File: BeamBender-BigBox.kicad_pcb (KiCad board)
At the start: 4 copper layers, 157.5 x 90 mm, 126 parts, among them CN1 A4000-CN621-36, CN2 A4000-CN622-54, J1 HDMI, J2 JTAG, J3 JTAG_Pogo, J4 EXT_BUTTONS, SW1 MENU, SW2 UP, SW3 DOWN, U1 Colorlight-i5-v7.0, U2 TLV76133DCYR, U3 74LVC16244ADGG, U4 74LVC16244ADGG, U5 SII9022ACNU, U6 74LVC1G86, U7 AK5720VT, U8 AP2112K-1.2, X1 Oscillator_3.2x2.5mm-27MHz, X2 Oscillator_5.0x3.2mm_24.576MHz

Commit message: Add R0/R1 pull down resistors
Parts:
- removed REF**: OSHW-Logo2_9.8x8mm_SilkScreen, Symbol:OSHW-Logo2_9.8x8mm_SilkScreen
- removed REF**: OSHW-Logo_11.4x12mm_SilkScreen, Symbol:OSHW-Logo_11.4x12mm_SilkScreen
- added R43: 100K, Resistor_SMD:R_0603_1608Metric, F.Cu at (133.2, 67.5)
- added R44: 100K, Resistor_SMD:R_0603_1608Metric, F.Cu at (133.2, 65.9)
- C18, C19: value 10uF X7R 1206 -> 10uF 1206
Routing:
- net R1: track 40.1 -> 45.3 mm
- net R0: track 40.0 -> 41.7 mm

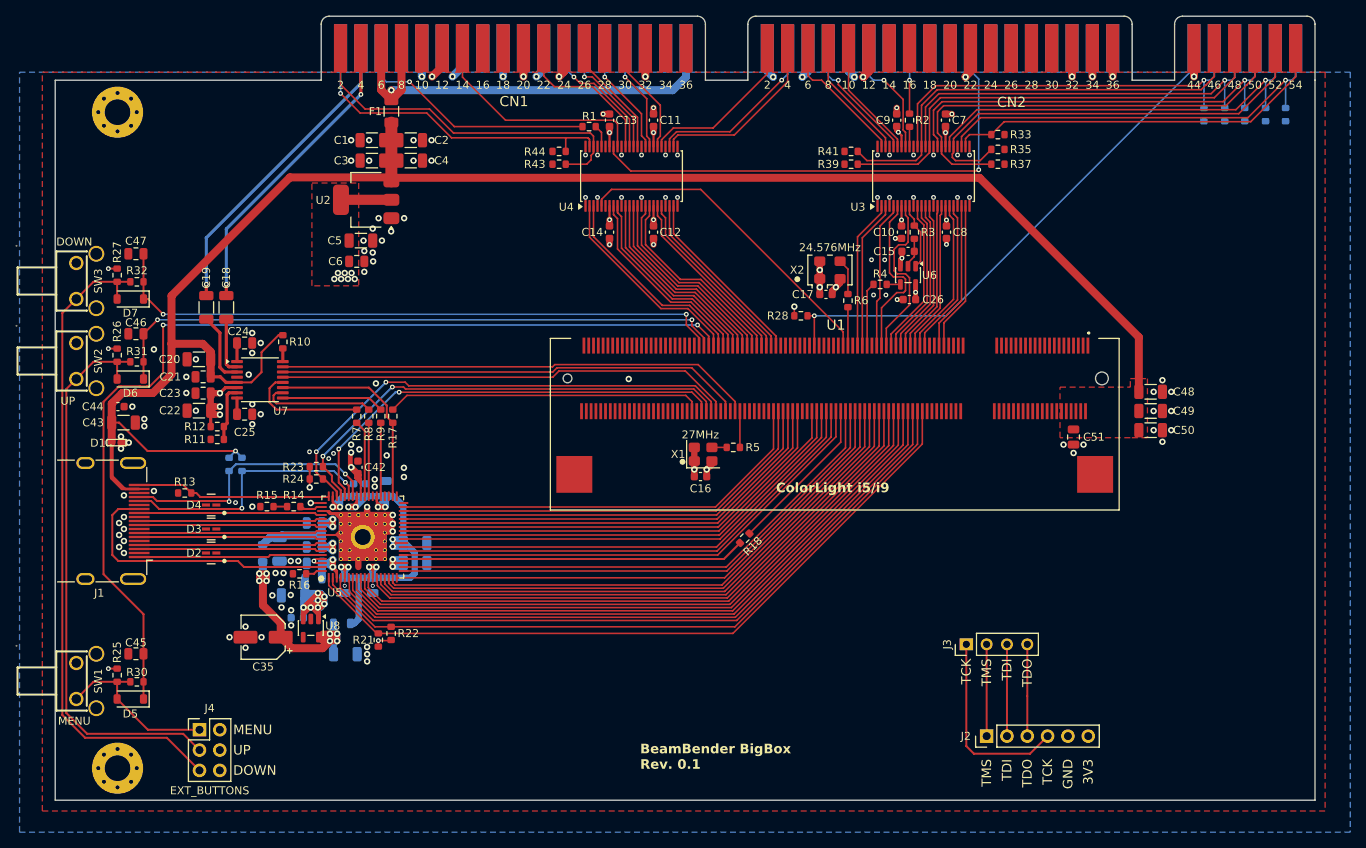
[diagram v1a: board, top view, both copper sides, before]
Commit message: Add EXT audio input mixed with Paula audio
External audio input via 3.5mm jack with an alternative 3 pin internal header mixed with Paula audio via OPA1692.
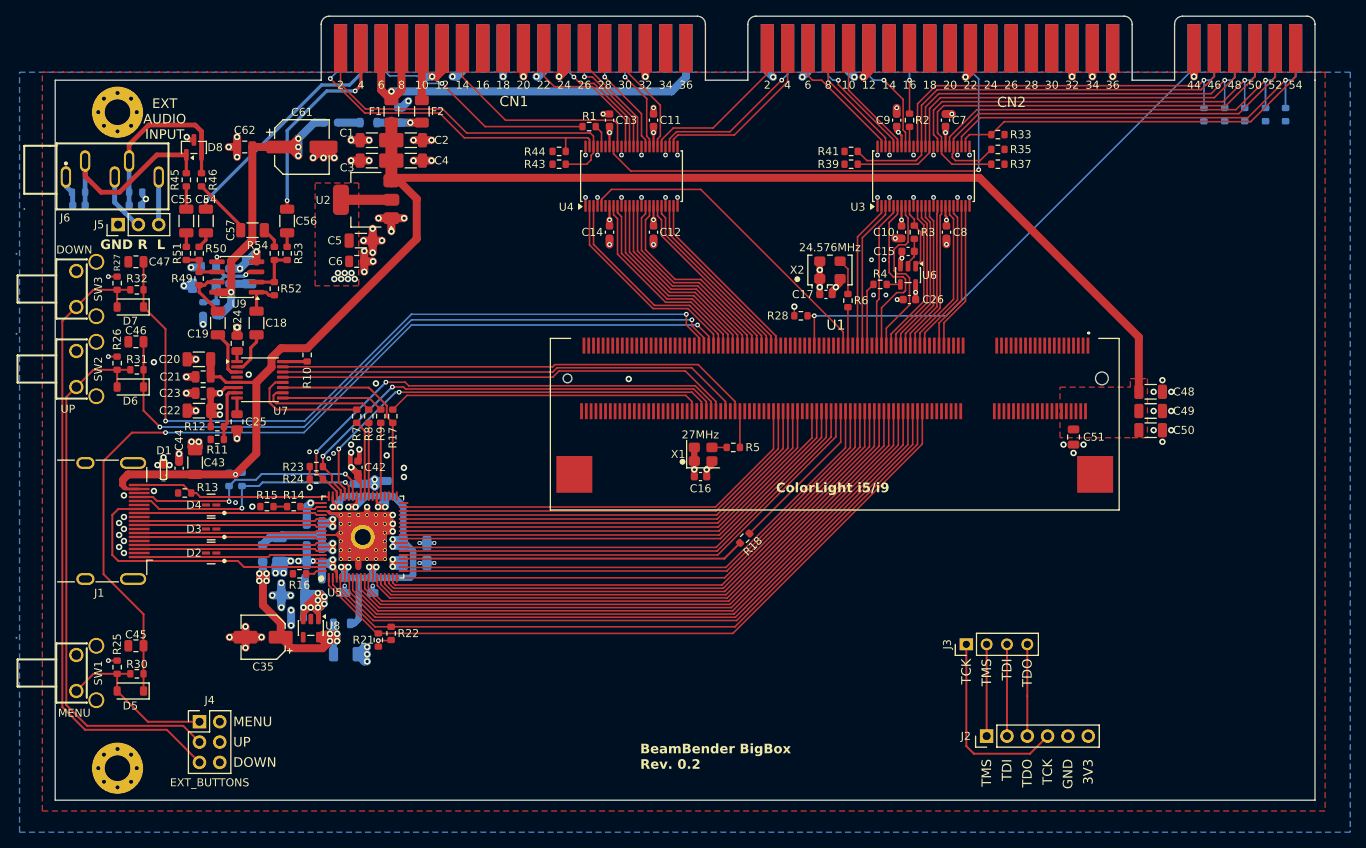
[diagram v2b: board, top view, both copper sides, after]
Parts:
- added C52: 330pF C0G, Capacitor_SMD:C_0603_1608Metric, B.Cu at (73.2, 72.7)
- added C53: 330pF C0G, Capacitor_SMD:C_0603_1608Metric, B.Cu at (80.2, 72.7)
- added C54: 10uF 1206, Capacitor_SMD:C_1206_3216Metric, F.Cu at (89.0, 74.6)
- added C55: 10uF 1206, Capacitor_SMD:C_1206_3216Metric, F.Cu at (86.6, 74.6)
- added C56: 10uF 1206, Capacitor_SMD:C_1206_3216Metric, F.Cu at (99.2, 74.6)
- added C57: 10uF 1206, Capacitor_SMD:C_1206_3216Metric, F.Cu at (94.9, 75.8)
- added C58: 22uF 1206, Capacitor_SMD:C_1206_3216Metric, B.Cu at (88.8, 82.7)
- added C59: 100nF 0805, Capacitor_SMD:C_0805_2012Metric, B.Cu at (89.4, 80.4)
- added C60: 100nF 0805, Capacitor_SMD:C_0805_2012Metric, B.Cu at (113.3, 61.4)
- added C61: 220uF 25V, Capacitor_SMD:CP_Elec_6.3x7.7, F.Cu at (101.0, 65.3)
- added C62: 100nF 0805, Capacitor_SMD:C_0805_2012Metric, F.Cu at (93.9, 65.3)
- added C63: 10uF 1206, Capacitor_SMD:C_1206_3216Metric, B.Cu at (94.5, 81.0)
- added C64: 100nF 0805, Capacitor_SMD:C_0805_2012Metric, B.Cu at (92.2, 81.5)
- added D8: TPD2E009, Package_TO_SOT_SMD:SOT-23, F.Cu at (87.5, 65.4)
- added F2: 0.1A, Fuse:Fuse_1206_3216Metric, F.Cu at (116.0, 60.9)
- added FB4: 600R@100MHz 0.5A, Inductor_SMD:L_0805_2012Metric, B.Cu at (109.4, 62.3)
- added J5: XAUDIO, Connector_PinHeader_2.54mm:PinHeader_1x03_P2.54mm_Vertical, F.Cu at (78.1, 75.0)
- added J6: SJ1-3535NG, BeamBenderFootprints:AUDIO-TH_SJ1-3535NG, F.Cu at (77.3, 68.1)
- added R29: 1K, Resistor_SMD:R_0603_1608Metric, B.Cu at (104.7, 62.3)
- added R45: 100, Resistor_SMD:R_0603_1608Metric, F.Cu at (86.6, 69.5)
- added R46: 100, Resistor_SMD:R_0603_1608Metric, F.Cu at (88.5, 69.5)
- added R47: 100K, Resistor_SMD:R_0603_1608Metric, B.Cu at (73.1, 71.0)
- added R48: 100K, Resistor_SMD:R_0603_1608Metric, B.Cu at (80.3, 71.0)
- added R49: 10K, Resistor_SMD:R_0603_1608Metric, F.Cu at (88.2, 81.8)
- added R50: 10K, Resistor_SMD:R_0603_1608Metric, F.Cu at (88.2, 78.7)
- added R51: 10K, Resistor_SMD:R_0603_1608Metric, F.Cu at (86.6, 78.7)
- added R52: 10K, Resistor_SMD:R_0603_1608Metric, F.Cu at (97.6, 83.1)
- added R53: 10K, Resistor_SMD:R_0603_1608Metric, F.Cu at (99.2, 78.7)
- added R54: 10K, Resistor_SMD:R_0603_1608Metric, F.Cu at (97.6, 78.7)
- added R55: 47K, Resistor_SMD:R_0603_1608Metric, B.Cu at (90.3, 85.6)
- added R56: 47K, Resistor_SMD:R_0603_1608Metric, B.Cu at (88.7, 85.6)
- added U9: OPA1692, Package_SO:SOIC-8_3.9x4.9mm_P1.27mm, F.Cu at (92.9, 81.6)
- moved C44 10.9 mm to (85.7, 105.5), turned to -90 degrees
- moved C43 10.3 mm to (87.7, 104.8), turned to -90 degrees
- moved D1 6.80 mm to (83.8, 105.7), turned to 90 degrees
- moved C18 4.25 mm to (95.4, 87.3)
- moved R10 3.45 mm to (101.7, 91.3)
- moved C19 2.43 mm to (90.5, 87.3)
- moved R19 1.88 mm to (92.0, 106.9)
- moved R20 1.88 mm to (93.5, 106.9)
- moved C25 1.34 mm to (92.9, 99.7), turned to -90 degrees
- moved C46 1.00 mm to (80.3, 89.7)
- moved C47 1.00 mm to (80.3, 79.7)
- moved D5 1.00 mm to (79.6, 133.3)
- moved D6 1.00 mm to (79.6, 95.3)
- moved D7 1.00 mm to (79.6, 85.3)
- moved J4 1.00 mm to (88.2, 137.2)
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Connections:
- C18 pad 1: R_AUDIO -> R_AUDMIX
- C19 pad 1: L_AUDIO -> L_AUDMIX
- CN1 pad 10: unconnected-(CN1-+12V-Pad10) -> 12V_IN
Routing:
- net GND: track 122.0 -> 227.0 mm, vias 152 -> 165
- net VA: track 0.00 -> 45.7 mm, vias 0 -> 4
- net VCC: track 234.0 -> 198.7 mm
- net Net-(D8-D+): track 0.00 -> 25.1 mm
- net Net-(D8-D-): track 0.00 -> 23.2 mm
- net BT3_INPUT: track 78.9 -> 96.2 mm
- net VBIAS: track 0.00 -> 13.0 mm, vias 0 -> 2
- net R_AUDIO: track 37.9 -> 26.0 mm
- net BT1_INPUT: track 124.1 -> 115.3 mm
- net L_AUDIO: track 38.9 -> 30.2 mm
- net BT2_INPUT: track 78.8 -> 87.4 mm
- net XAUDR: track 0.00 -> 7.50 mm
- net XAUDESDR: track 0.00 -> 7.33 mm
- net L_AUDMIX: track 0.00 -> 6.64 mm
- net Net-(U9A--): track 0.00 -> 6.59 mm
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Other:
- board text added: "BeamBender BigBox Rev. 0.2"
- board text added: "EXT AUDIO INPUT"
- board text added: "GND R L"
- board text removed: "BeamBender BigBox Rev. 0.1"

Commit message: Add HDMI back-feed protection
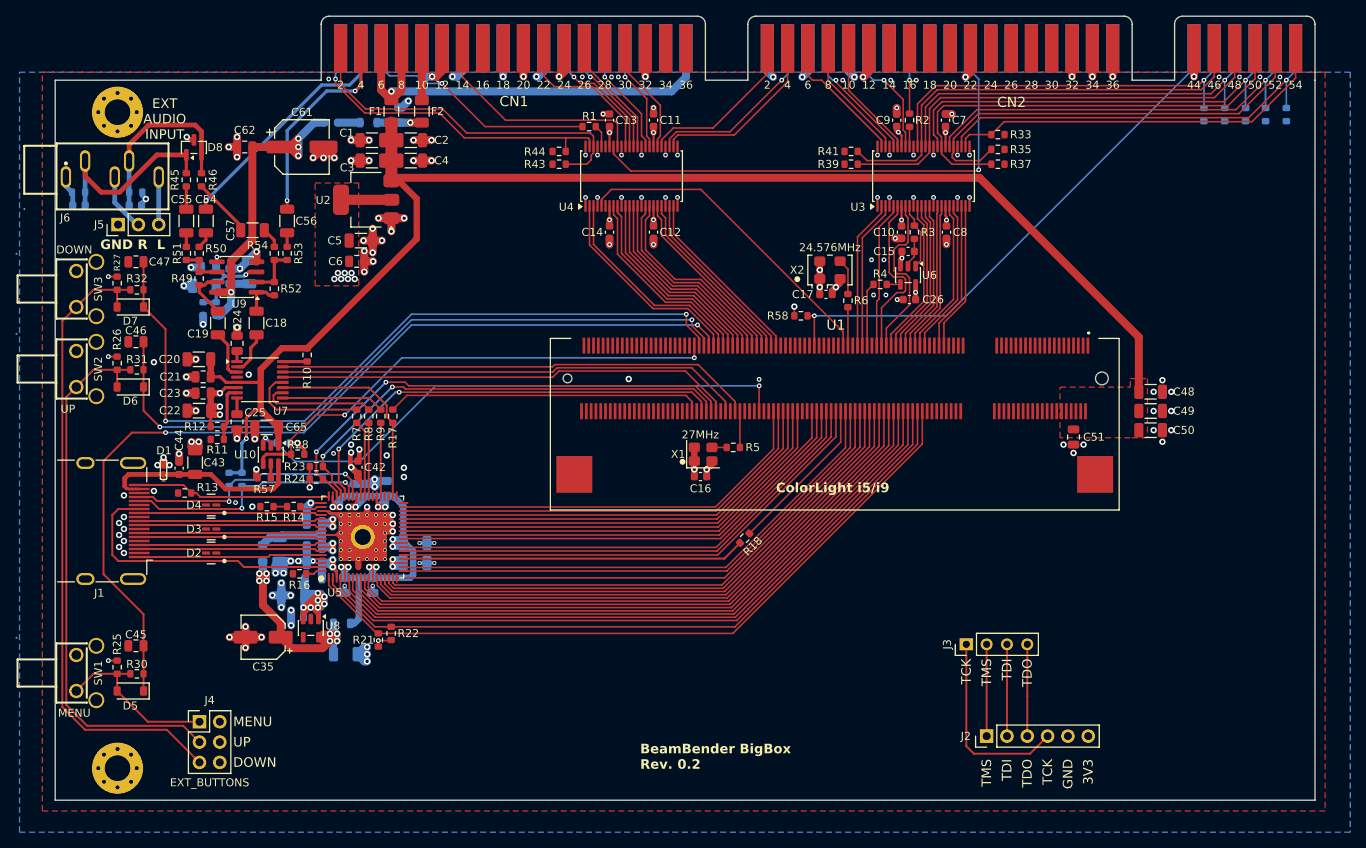
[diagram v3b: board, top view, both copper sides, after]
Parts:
- added C65: 10uF 1206, Capacitor_SMD:C_1206_3216Metric, F.Cu at (96.6, 100.4)
- added R28: 100K, Resistor_SMD:R_0603_1608Metric, F.Cu at (100.5, 103.8)
- added R29: 10K, Resistor_SMD:R_0603_1608Metric, B.Cu at (98.7, 102.3)
- added R57: 56K, Resistor_SMD:R_0603_1608Metric, F.Cu at (96.3, 106.7)
- added U10: TPS2553DBVR, Package_TO_SOT_SMD:SOT-23-6, F.Cu at (97.2, 103.8)
- moved R34 0.10 mm to (224.1, 61.3)
- moved R38 0.10 mm to (219.0, 61.3)
- renumbered R28 to R58, R29 to R59
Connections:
- C43 pad 2: VCC -> HDMI_5V
- C44 pad 2: VCC -> HDMI_5V
- D1 pad 1: VCC -> HDMI_5V
- J1 pad 18: VCC -> HDMI_5V
- U1 pad 126: unconnected-(U1-F4/PL11A-Pad126) -> HDMI_EN
- U1 pad 153: unconnected-(U1-E1/PL17D-Pad153) -> HDMI_FAULT
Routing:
- net HDMI_EN: track 0.00 -> 71.1 mm, vias 0 -> 2
- net HDMI_FAULT: track 0.00 -> 62.4 mm, vias 0 -> 2
- net HDMI_5V: track 0.00 -> 28.0 mm
- net VCC: track 198.7 -> 182.2 mm
- net 3V3: track 99.0 -> 101.7 mm, vias 35 -> 36
- net GND: track 227.0 -> 229.6 mm, vias 165 -> 176
- net Net-(U10-ILIM): track 0.00 -> 1.76 mm
- net R0: track 42.5 -> 41.9 mm
- net G0: track 52.2 -> 51.7 mm
